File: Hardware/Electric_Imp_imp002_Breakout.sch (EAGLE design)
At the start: 41 parts, among them Q1 DMG2307L-7, Q2 PHOTOTRANSISTORPT17-21C-L41-T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, U1 imp002, U2 TPS62172, X1 USBSMD

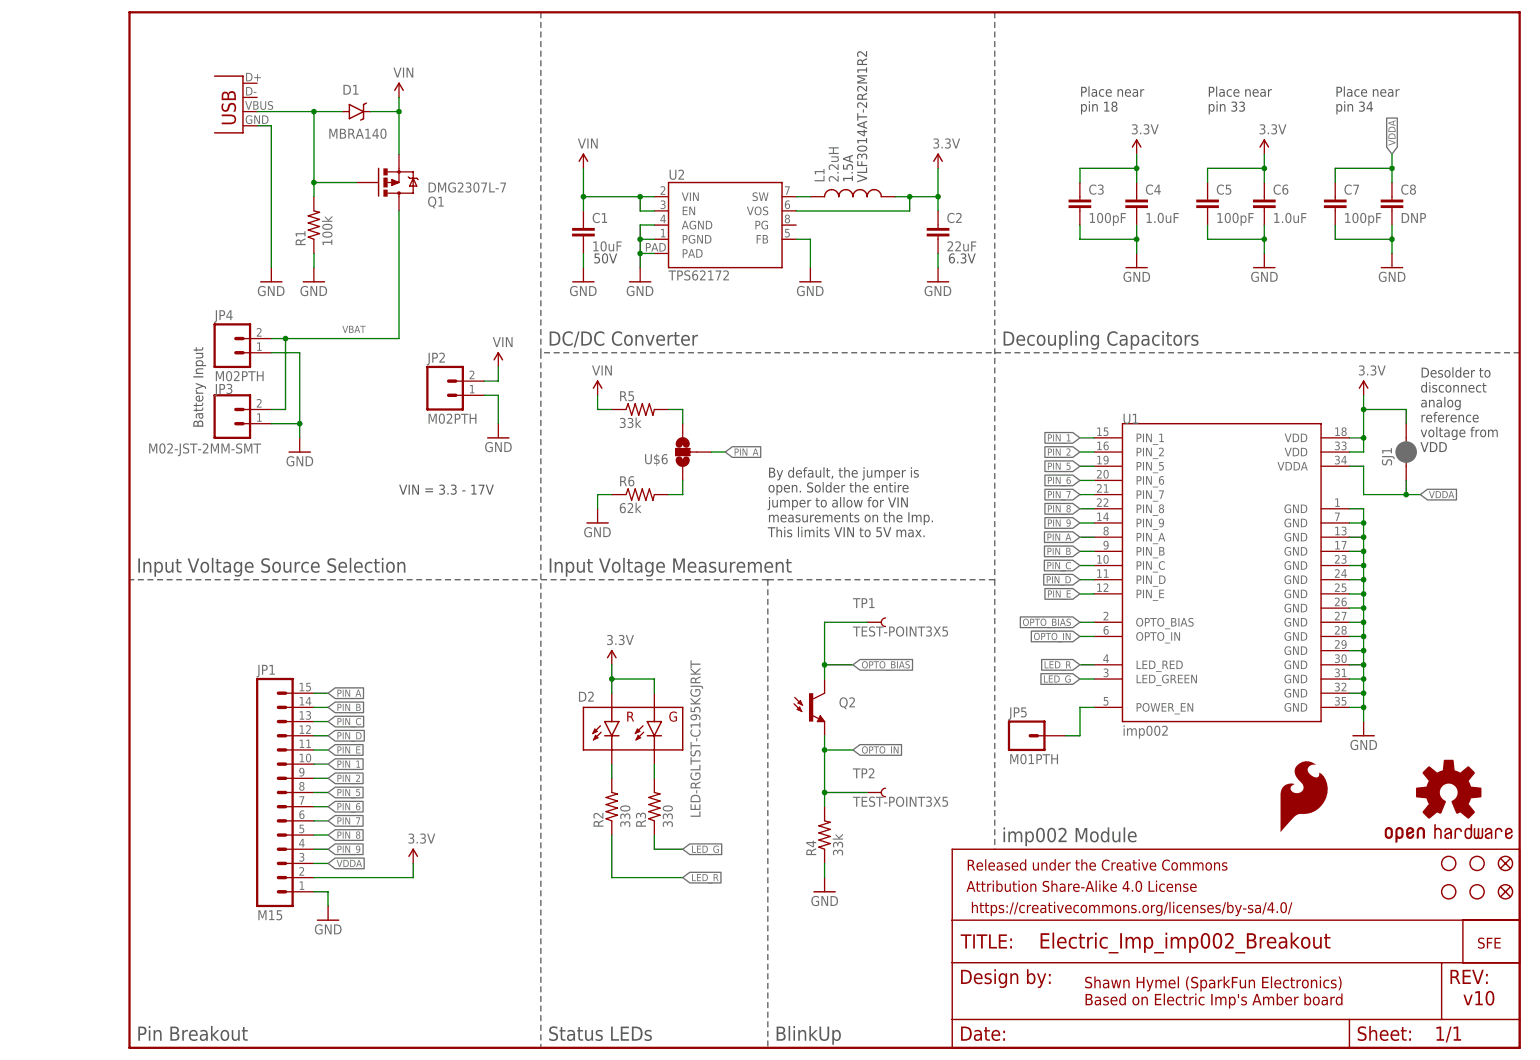
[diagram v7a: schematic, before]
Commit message: Added 10k pullup on LED_R line. Added warning notes to the solder jumpers.
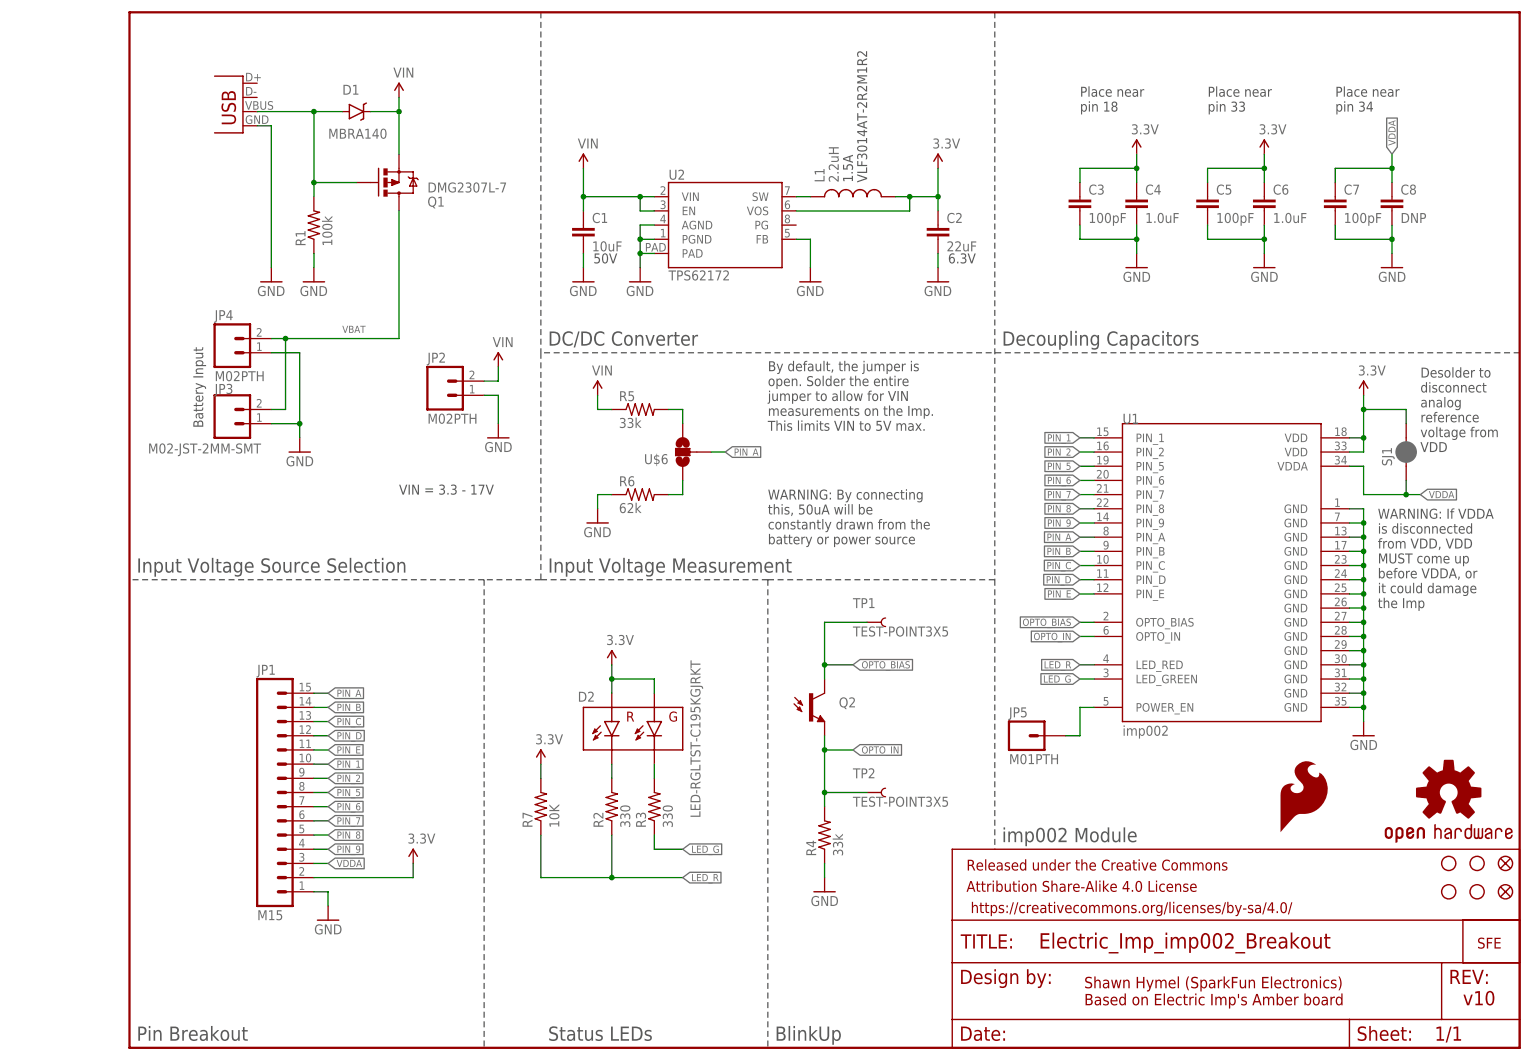
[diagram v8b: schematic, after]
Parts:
- added R7: 10K, SparkFun-Resistors:10KOHM1/10W1%(0603)0603
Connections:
- net 3.3V: now also R7.2
- net LED_R: now also R7.1
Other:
- note added: "WARNING: By connecting this, 50uA will be constantly drawn from the battery or power source"
- note added: "WARNING: If VDDA is disconnected from VDD, VDD MUST come up before VDDA, or it could damage the Imp"
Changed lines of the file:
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@@
 <setting verticaltext="up"/>
 </settings>
-<grid distance="0.1" unitdist="inch" unit="inch" style="lines" multiple="1" display="no" altdistance="0.01" altunitdist="inch" altunit="inch"/>
+<grid distance="0.1" unitdist="inch" unit="inch" style="lines" multiple="1" display="yes" altdistance="0.01" altunitdist="inch" altunit="inch"/>
 <layers>
 <layer number="1" name="Top" color="4" fill="1" visible="no" active="no"/>
@@
 <part name="LOGO1" library="SparkFun-Aesthetics" deviceset="OSHW-LOGO" device="S"/>
 <part name="LOGO2" library="SparkFun-Aesthetics" deviceset="SFE_LOGO_FLAME" device=".1_INCH"/>
+<part name="R7" library="SparkFun-Resistors" deviceset="10KOHM1/10W1%(0603)" device="0603" value="10K"/>
+<part name="P+4" library="SparkFun-Aesthetics" deviceset="3.3V" device=""/>
 </parts>
 <sheets>
@@
 <wire x1="154.94" y1="83.82" x2="154.94" y2="35.56" width="0.1524" layer="97" style="longdash"/>
 <wire x1="154.94" y1="83.82" x2="114.3" y2="83.82" width="0.1524" layer="97" style="longdash"/>
-<wire x1="114.3" y1="83.82" x2="0" y2="83.82" width="0.1524" layer="97" style="longdash"/>
+<wire x1="114.3" y1="83.82" x2="73.66" y2="83.82" width="0.1524" layer="97" style="longdash"/>
+<wire x1="73.66" y1="83.82" x2="63.5" y2="83.82" width="0.1524" layer="97" style="longdash"/>
+<wire x1="63.5" y1="83.82" x2="0" y2="83.82" width="0.1524" layer="97" style="longdash"/>
 <wire x1="248.92" y1="124.46" x2="73.66" y2="124.46" width="0.1524" layer="97" style="longdash"/>
 <text x="1.27" y="85.09" size="2.54" layer="97">Input Voltage Source Selection</text>
@@
 <text x="156.21" y="36.83" size="2.54" layer="97">imp002 Module</text>
 <text x="1.27" y="1.27" size="2.54" layer="97">Pin Breakout</text>
-<wire x1="73.66" y1="124.46" x2="73.66" y2="0" width="0.1524" layer="97" style="longdash"/>
+<wire x1="73.66" y1="124.46" x2="73.66" y2="83.82" width="0.1524" layer="97" style="longdash"/>
 <wire x1="114.3" y1="83.82" x2="114.3" y2="0" width="0.1524" layer="97" style="longdash"/>
 <text x="74.93" y="1.27" size="2.54" layer="97">Status LEDs</text>
 <text x="115.57" y="1.27" size="2.54" layer="97">BlinkUp</text>
-<text x="114.3" y="91.44" size="1.778" layer="97">By default, the jumper is
+<text x="114.3" y="110.49" size="1.778" layer="97">By default, the jumper is
 open. Solder the entire
 jumper to allow for VIN
@@
 <text x="238.76" y="7.62" size="2.54" layer="94">v10</text>
 <text x="48.26" y="99.06" size="1.778" layer="97">VIN = 3.3 - 17V</text>
+<wire x1="63.5" y1="83.82" x2="63.5" y2="0" width="0.1524" layer="97" style="longdash"/>
+<text x="114.3" y="90.17" size="1.778" layer="97">WARNING: By connecting
+this, 50uA will be
+constantly drawn from the
+battery or power source</text>
+<text x="223.52" y="78.74" size="1.778" layer="97">WARNING: If VDDA
+is disconnected
+from VDD, VDD
+MUST come up
+before VDDA, or
+it could damage
+the Imp</text>
 </plain>
 <instances>
@@
 <instance part="LOGO1" gate="G$1" x="236.22" y="45.72"/>
 <instance part="LOGO2" gate="G$1" x="205.74" y="38.1"/>
+<instance part="R7" gate="G$1" x="73.66" y="43.18" rot="R90"/>
+<instance part="P+4" gate="G$1" x="73.66" y="50.8"/>
 </instances>
 <busses>
@@
 <pinref part="P+7" gate="G$1" pin="3.3V"/>
 </segment>
+<segment>
+<pinref part="R7" gate="G$1" pin="2"/>
+<pinref part="P+4" gate="G$1" pin="3.3V"/>
+<wire x1="73.66" y1="48.26" x2="73.66" y2="50.8" width="0.1524" layer="91"/>
+</segment>
 </net>
 <net name="VIN" class="0">
@@
 <wire x1="86.36" y1="30.48" x2="99.06" y2="30.48" width="0.1524" layer="91"/>
 <label x="99.06" y="30.48" size="1.27" layer="95" xref="yes"/>
-</segment>
-</net>
+<wire x1="86.36" y1="30.48" x2="73.66" y2="30.48" width="0.1524" layer="91"/>
+<junction x="86.36" y="30.48"/>
+<pinref part="R7" gate="G$1" pin="1"/>
+<wire x1="73.66" y1="30.48" x2="73.66" y2="38.1" width="0.1524" layer="91"/>
+</segment>
+</net>
